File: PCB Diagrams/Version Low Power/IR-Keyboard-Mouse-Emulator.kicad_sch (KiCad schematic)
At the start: 25 parts, among them J1 USB_A, J2 01x02, Q1 BC557, Q2 BC557, Q3 BC547, Q4 BC547, U1 Arduino_Pro_Micro, U2 VS1838B

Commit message: Adding Low Power protoboard & schematics diagram
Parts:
- renumbered D3 to D1, D1 to D2, D2 to D3, Q3 to Q2, Q2 to Q3, R5 to R1, R1 to R2, R2 to R3, R3 to R5, R7 to R6, R6 to R7
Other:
- moved on the sheet: C1, D1, D2, D3, D4, H1, H2, H3, H4, Q1, Q2, Q3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

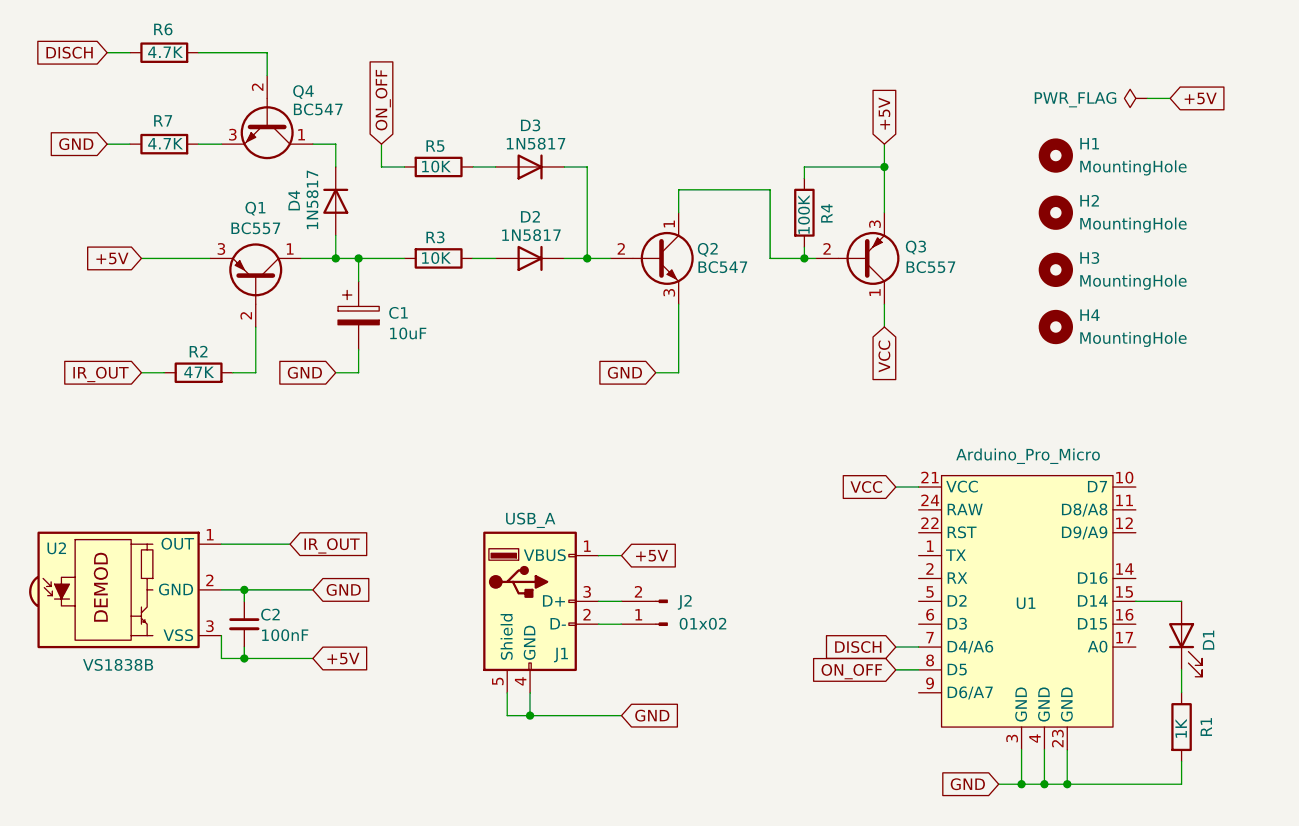
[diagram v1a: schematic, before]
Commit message: Adding low-power firmware
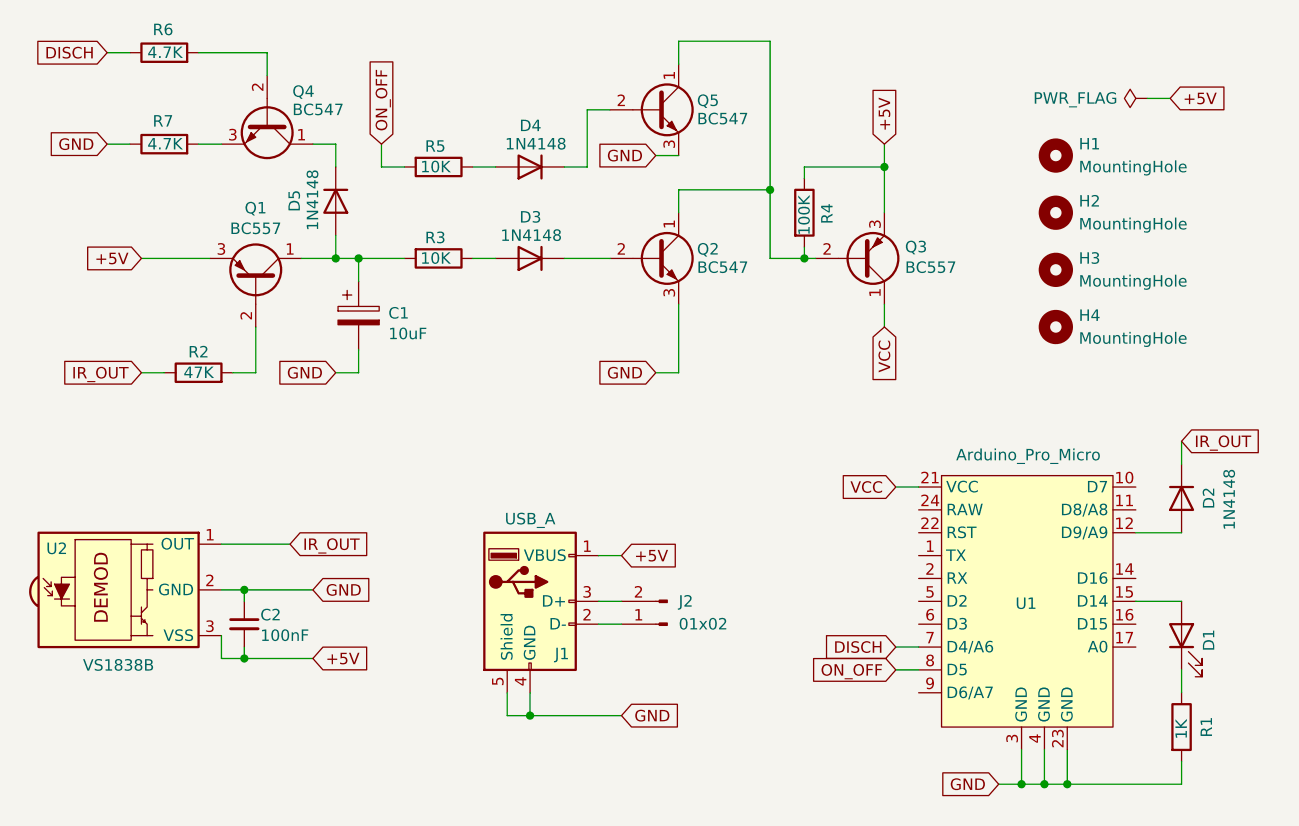
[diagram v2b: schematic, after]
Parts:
- added D2: 1N4148, Diode_THT:D_DO-35_SOD27_P7.62mm_Horizontal, symbol Device:D
- added Q5: BC547, Package_TO_SOT_THT:TO-92_Inline_Wide, symbol Transistor_BJT:BC547
- D3: renamed from D2; value 1N5817 -> 1N4148
- D4: renamed from D3; value 1N5817 -> 1N4148
- D5: renamed from D4; value 1N5817 -> 1N4148
- Q1, Q2, Q3, Q4: footprint Package_TO_SOT_THT:TO-92_Inline -> Package_TO_SOT_THT:TO-92_Inline_Wide
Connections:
- net GND: now also Q5.3 (E)
- net IR_OUT: now also D2.1 (K)
- net at U1.12 (D9/A9): now also D2.2 (A)
- net at Q2.1 (C), Q3.2 (B), R4.2: now also Q5.1 (C)
- net at D3.1 (K), Q2.2 (B): no longer D4.1 (K)
- new net: D4.1 (K), Q5.2 (B)

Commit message: Adding low-power version PCB
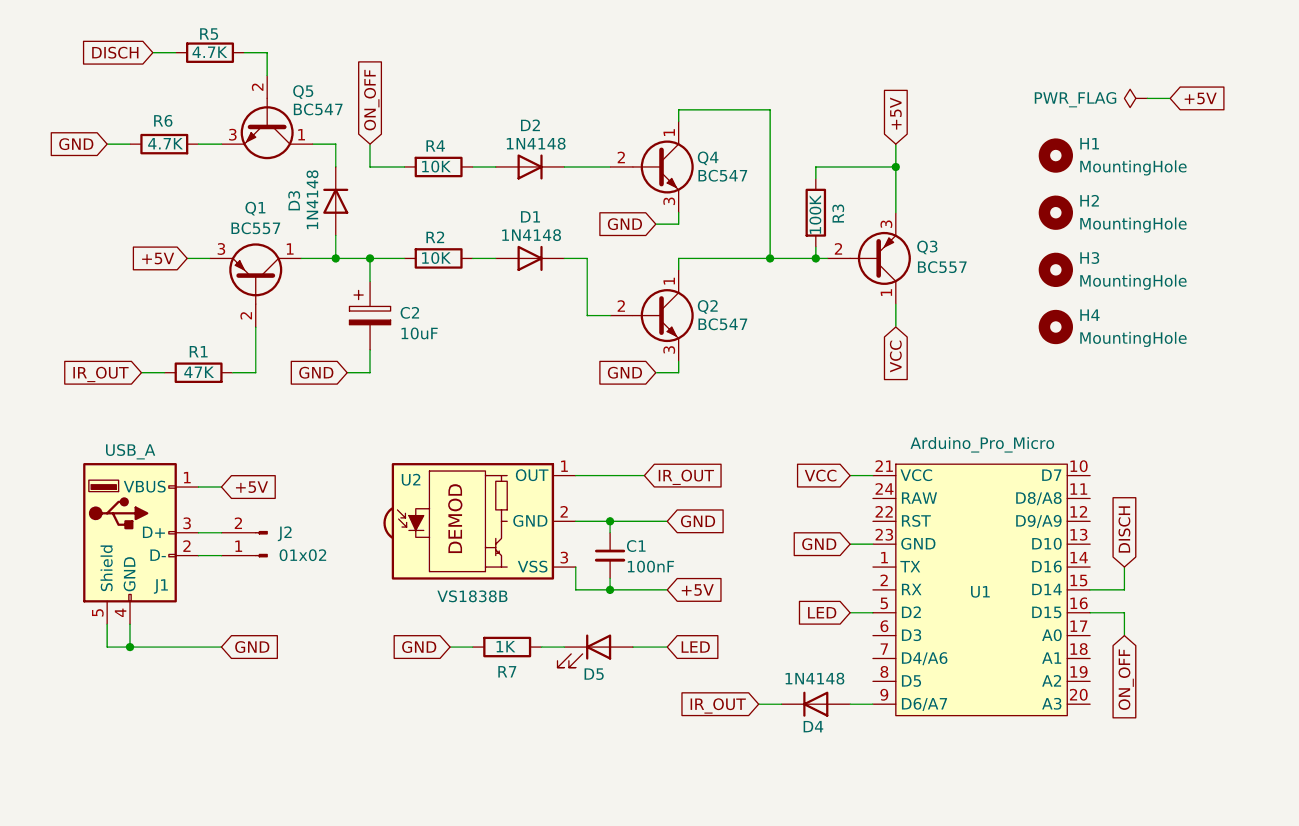
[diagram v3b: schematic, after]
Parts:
- R1: renamed from R2; footprint Resistor_THT:R_Axial_DIN0207_L6.3mm_D2.5mm_P5.08mm_Vertical -> Resistor_THT:R_Axial_DIN0207_L6.3mm_D2.5mm_P2.54mm_Vertical
- R2: renamed from R3; footprint Resistor_THT:R_Axial_DIN0207_L6.3mm_D2.5mm_P5.08mm_Vertical -> Resistor_THT:R_Axial_DIN0207_L6.3mm_D2.5mm_P2.54mm_Vertical
- R3: renamed from R4; footprint Resistor_THT:R_Axial_DIN0207_L6.3mm_D2.5mm_P5.08mm_Vertical -> Resistor_THT:R_Axial_DIN0207_L6.3mm_D2.5mm_P2.54mm_Vertical
- R4: renamed from R5; footprint Resistor_THT:R_Axial_DIN0207_L6.3mm_D2.5mm_P5.08mm_Vertical -> Resistor_THT:R_Axial_DIN0207_L6.3mm_D2.5mm_P2.54mm_Vertical
- R5: renamed from R6; footprint Resistor_THT:R_Axial_DIN0207_L6.3mm_D2.5mm_P5.08mm_Vertical -> Resistor_THT:R_Axial_DIN0207_L6.3mm_D2.5mm_P2.54mm_Vertical
- R6: renamed from R7; footprint Resistor_THT:R_Axial_DIN0207_L6.3mm_D2.5mm_P5.08mm_Vertical -> Resistor_THT:R_Axial_DIN0207_L6.3mm_D2.5mm_P2.54mm_Vertical
- R7: renamed from R1; footprint Resistor_THT:R_Axial_DIN0207_L6.3mm_D2.5mm_P5.08mm_Vertical -> Resistor_THT:R_Axial_DIN0204_L3.6mm_D1.6mm_P7.62mm_Horizontal
- renumbered C2 to C1, C1 to C2, D3 to D1, D4 to D2, D5 to D3, D2 to D4, D1 to D5, Q5 to Q4, Q4 to Q5
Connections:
- net DISCH: now also R5.2, U1.15 (D14); no longer R5.1, U1.7 (D4/A6)
- net ON_OFF: now also U1.16 (D15); no longer U1.8 (D5)
- net at D4.2 (A): now also U1.9 (D6/A7); no longer U1.12 (D9/A9)
- net LED: now reaches D5.2 (A)
- net LED: now also U1.5 (D2); no longer U1.15 (D14)
- net at Q5.2 (B): now also R5.1; no longer R5.2
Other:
- moved on the sheet: C1, C2, D4, D5, J1, J2, Q2, Q3, Q4, R3, R5, R7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
